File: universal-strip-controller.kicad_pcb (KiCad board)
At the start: 4 copper layers, 200 x 125 mm, 242 parts, among them J1 Conn_01x03_Pin, J10 DB301V-3.5-3P-GN, J11 DB301V-3.5-3P-GN, J12 DB301V-3.5-3P-GN, J13 DB301V-3.5-3P-GN, J14 DB301V-3.5-3P-GN, J15 DB301V-3.5-3P-GN, J16 DB301V-3.5-3P-GN, J17 DB301V-3.5-3P-GN, J18 DB301V-3.5-3P-GN, J19 DB301V-3.5-3P-GN, J2 Conn_01x02_Pin, J20 DB301V-3.5-3P-GN, J21 DB301V-3.5-3P-GN, J22 DB301V-3.5-3P-GN, J23 DB301V-3.5-3P-GN, J24 DB301V-3.5-3P-GN, J25 DB301V-3.5-3P-GN, J26 DB301V-3.5-3P-GN, J27 DB301V-3.5-3P-GN, J28 DB301V-3.5-3P-GN, J29 DB301V-3.5-3P-GN, J3 DBT50G-9.5-2P, J30 DB301V-3.5-3P-GN, J31 DB301V-3.5-3P-GN, J32 DB301V-3.5-3P-GN, J33 DB301V-3.5-3P-GN, J34 DB301V-3.5-3P-GN, J35 DB301V-3.5-3P-GN, J36 DB301V-3.5-3P-GN, J37 DB301V-3.5-3P-GN, J38 2.54-1*4, J39 DB301V-3.5-3P-GN, J4 DBT50G-9.5-2P, J5 DBT50G-9.5-2P, J6 DBT50G-9.5-2P, J7 DB301V-3.5-3P-GN, J8 DB301V-3.5-3P-GN, J9 DB301V-3.5-3P-GN, SW1 434133025816, SW2 434133025816, U1 RP2350B, U10 SN74LVC8T245PWR, U11 SN74LVC8T245PWR, U2 RPI RM2, U3 W25Q128JVSIQ, U4 SN74LVC1T45DBV, U5 TPS63070RNMR, U7 SN74LVC8T245PWR, U8 SN74LVC8T245PWR, U9 DS3231SN, X1 12MHz

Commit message: Some changes, not sure what...
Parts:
- moved D5 233.7 mm to (215.6, 57.2)
- moved D6 233.7 mm to (215.6, 61.8)
- moved D7 233.7 mm to (215.6, 66.3)
- moved D8 233.7 mm to (215.6, 70.9)
- moved BT1 17.3 mm to (194.2, 121.1)
- moved C118 17.3 mm to (172.8, 116.5)
- moved R95 17.3 mm to (191.6, 113.3)
- moved R96 17.3 mm to (172.8, 113.0)
- moved U9 17.3 mm to (180.5, 120.0)
- moved R94 17.3 mm to (188.3, 113.3)
- moved R49 10.8 mm to (154.9, 121.3)
- moved R50 10.8 mm to (156.5, 121.3)
- moved R53 10.8 mm to (161.4, 121.3)
- moved R54 10.8 mm to (163.0, 121.3)
- moved R47 10.8 mm to (151.6, 121.3)
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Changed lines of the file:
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@@
 		(capping no)
 		(filling no)
-		(zone_defaults)
 		(pcbplotparams
 			(layerselection 0x00000000_00000000_55555555_5755f5ff)
@@
 	(footprint "PCM_JLCPCB:D_SMA"
 		(layer "F.Cu")
-		(at -18.045 57.825)
+		(at 215.6 61.8)
 		(descr "Diode SMA (DO-214AC)")
 		(tags "Diode SMA (DO-214AC)")
@@
 	(footprint "PixelBlit:R_0603"
 		(layer "F.Cu")
-		(at 208.1 108.06 90)
+		(at 191.6 113.34 90)
 		(descr "Resistor SMD 0603 (1608 Metric), square (rectangular) end terminal, IPC_7351 nominal, (Body size source: IPC-SM-782 page 72, https://www.pcb-3d.com/wordpress/wp-content/uploads/ipc-sm-782a_amendment_1_and_2.pdf), generated with kicad-footprint-generator")
 		(tags "resistor")
@@
 	(footprint "PixelBlit:R_0603"
 		(layer "F.Cu")
-		(at 189.3 107.71 90)
+		(at 172.8 112.99 90)
 		(descr "Resistor SMD 0603 (1608 Metric), square (rectangular) end terminal, IPC_7351 nominal, (Body size source: IPC-SM-782 page 72, https://www.pcb-3d.com/wordpress/wp-content/uploads/ipc-sm-782a_amendment_1_and_2.pdf), generated with kicad-footprint-generator")
 		(tags "resistor")
@@
 	(footprint "PixelBlit:R_0402"
 		(layer "F.Cu")
-		(at 100.428571 121.45 -90)
+		(at 105.578571 120.75 -90)
 		(descr "Resistor SMD 0402 (1005 Metric), square (rectangular) end terminal, IPC_7351 nominal, (Body size source: IPC-SM-782 page 72, https://www.pcb-3d.com/wordpress/wp-content/uploads/ipc-sm-782a_amendment_1_and_2.pdf), generated with kicad-footprint-generator")
 		(tags "resistor")
@@
 	(footprint "PixelBlit:R_0402"
 		(layer "F.Cu")
-		(at 163.938583 122.98 -90)
+		(at 153.238583 121.33 -90)
 		(descr "Resistor SMD 0402 (1005 Metric), square (rectangular) end terminal, IPC_7351 nominal, (Body size source: IPC-SM-782 page 72, https://www.pcb-3d.com/wordpress/wp-content/uploads/ipc-sm-782a_amendment_1_and_2.pdf), generated with kicad-footprint-generator")
 		(tags "resistor")
@@
 	(footprint "PixelBlit:R_0402"
 		(layer "F.Cu")
-		(at 105.95 121.45 -90)
+		(at 111.1 120.75 -90)
 		(descr "Resistor SMD 0402 (1005 Metric), square (rectangular) end terminal, IPC_7351 nominal, (Body size source: IPC-SM-782 page 72, https://www.pcb-3d.com/wordpress/wp-content/uploads/ipc-sm-782a_amendment_1_and_2.pdf), generated with kicad-footprint-generator")
 		(tags "resistor")
@@
 	(footprint "PCM_JLCPCB:D_SMA"
 		(layer "F.Cu")
-		(at -18.045 62.375)
+		(at 215.6 66.35)
 		(descr "Diode SMA (DO-214AC)")
 		(tags "Diode SMA (DO-214AC)")
@@
 	(footprint "PixelBlit:R_0402"
 		(layer "F.Cu")
-		(at 165.567155 122.98 -90)
+		(at 154.867155 121.33 -90)
 		(descr "Resistor SMD 0402 (1005 Metric), square (rectangular) end terminal, IPC_7351 nominal, (Body size source: IPC-SM-782 page 72, https://www.pcb-3d.com/wordpress/wp-content/uploads/ipc-sm-782a_amendment_1_and_2.pdf), generated with kicad-footprint-generator")
 		(tags "resistor")
@@
 	(footprint "PixelBlit:R_0402"
 		(layer "F.Cu")
-		(at 104.55 121.45 -90)
+		(at 109.7 120.75 -90)
 		(descr "Resistor SMD 0402 (1005 Metric), square (rectangular) end terminal, IPC_7351 nominal, (Body size source: IPC-SM-782 page 72, https://www.pcb-3d.com/wordpress/wp-content/uploads/ipc-sm-782a_amendment_1_and_2.pdf), generated with kicad-footprint-generator")
 		(tags "resistor")
@@
 	(footprint "PixelBlit:R_0402"
 		(layer "F.Cu")
-		(at 108.8 121.45 -90)
+		(at 113.95 120.75 -90)
 		(descr "Resistor SMD 0402 (1005 Metric), square (rectangular) end terminal, IPC_7351 nominal, (Body size source: IPC-SM-782 page 72, https://www.pcb-3d.com/wordpress/wp-content/uploads/ipc-sm-782a_amendment_1_and_2.pdf), generated with kicad-footprint-generator")
 		(tags "resistor")
@@
 	(footprint "PixelBlit:R_0402"
 		(layer "F.Cu")
-		(at 168.824298 122.98 -90)
+		(at 158.124298 121.33 -90)
 		(descr "Resistor SMD 0402 (1005 Metric), square (rectangular) end terminal, IPC_7351 nominal, (Body size source: IPC-SM-782 page 72, https://www.pcb-3d.com/wordpress/wp-content/uploads/ipc-sm-782a_amendment_1_and_2.pdf), generated with kicad-footprint-generator")
 		(tags "resistor")
@@
 	(footprint "PixelBlit:R_0402"
 		(layer "F.Cu")
-		(at 101.907143 121.45 -90)
+		(at 107.057143 120.75 -90)
 		(descr "Resistor SMD 0402 (1005 Metric), square (rectangular) end terminal, IPC_7351 nominal, (Body size source: IPC-SM-782 page 72, https://www.pcb-3d.com/wordpress/wp-content/uploads/ipc-sm-782a_amendment_1_and_2.pdf), generated with kicad-footprint-generator")
 		(tags "resistor")
@@
 	(footprint "Package_SO:SOIC-16W_7.5x10.3mm_P1.27mm"
 		(layer "F.Cu")
-		(at 197 114.745)
+		(at 180.5 120.025)
 		(descr "SOIC, 16 Pin (JEDEC MS-013AA, https://www.analog.com/media/en/package-pcb-resources/package/pkg_pdf/soic_wide-rw/rw_16.pdf)")
 		(tags "SOIC SO")
@@
 	(footprint "PixelBlit:R_0402"
 		(layer "F.Cu")
-		(at 167.195726 122.98 -90)
+		(at 156.495726 121.33 -90)
 		(descr "Resistor SMD 0402 (1005 Metric), square (rectangular) end terminal, IPC_7351 nominal, (Body size source: IPC-SM-782 page 72, https://www.pcb-3d.com/wordpress/wp-content/uploads/ipc-sm-782a_amendment_1_and_2.pdf), generated with kicad-footprint-generator")
 		(tags "resistor")
@@
 	(footprint "PixelBlit:R_0402"
 		(layer "F.Cu")
-		(at 98.95 121.45 -90)
+		(at 104.1 120.75 -90)
 		(descr "Resistor SMD 0402 (1005 Metric), square (rectangular) end terminal, IPC_7351 nominal, (Body size source: IPC-SM-782 page 72, https://www.pcb-3d.com/wordpress/wp-content/uploads/ipc-sm-782a_amendment_1_and_2.pdf), generated with kicad-footprint-generator")
 		(tags "resistor")
@@
 	(footprint "PixelBlit:VQFN-HR-15_L3.0-W2.5-P0.50-BL_TPS63070RNMR"
 		(layer "F.Cu")
-		(at -19.02 116.655)
+		(at -14.45 119.88)
 		(property "Reference" "U5"
 			(at -2.75 -1.57 90)
@@
 	(footprint "PCM_JLCPCB:D_SMA"
 		(layer "F.Cu")
-		(at -18.045 53.275)
+		(at 215.6 57.25)
 		(descr "Diode SMA (DO-214AC)")
 		(tags "Diode SMA (DO-214AC)")
@@
 	(footprint "PixelBlit:R_0402"
 		(layer "F.Cu")
-		(at 172.081441 122.98 -90)
+		(at 161.381441 121.33 -90)
 		(descr "Resistor SMD 0402 (1005 Metric), square (rectangular) end terminal, IPC_7351 nominal, (Body size source: IPC-SM-782 page 72, https://www.pcb-3d.com/wordpress/wp-content/uploads/ipc-sm-782a_amendment_1_and_2.pdf), generated with kicad-footprint-generator")
 		(tags "resistor")
@@
 	(footprint "PixelBlit:R_0402"
 		(layer "F.Cu")
-		(at 107.3 121.45 -90)
+		(at 112.45 120.75 -90)
 		(descr "Resistor SMD 0402 (1005 Metric), square (rectangular) end terminal, IPC_7351 nominal, (Body size source: IPC-SM-782 page 72, https://www.pcb-3d.com/wordpress/wp-content/uploads/ipc-sm-782a_amendment_1_and_2.pdf), generated with kicad-footprint-generator")
 		(tags "resistor")
@@
 	(footprint "PixelBlit:C_0402"
 		(layer "F.Cu")
-		(at 189.3 111.2 90)
+		(at 172.8 116.48 90)
 		(descr "Capacitor SMD 0402 (1005 Metric), square (rectangular) end terminal, IPC_7351 nominal, (Body size source: IPC-SM-782 page 76, https://www.pcb-3d.com/wordpress/wp-content/uploads/ipc-sm-782a_amendment_1_and_2.pdf), generated with kicad-footprint-generator")
 		(tags "capacitor")
@@
 	(footprint "PixelBlit:TSSOP-24_L7.8-W4.4-P0.65-LS6.4-BL"
 		(layer "F.Cu")
-		(at 167.440012 114.2 180)
+		(at 156.740012 112.55 180)
 		(property "Reference" "U11"
 			(at -4.95 -2.64 90)
@@
 	(footprint "KiCad_Standard:Battery_Panasonic_CR1220-VCN_Vertical_CircularHoles"
 		(layer "F.Cu")
-		(at 210.75 115.85)
+		(at 194.25 121.13)
 		(descr "Panasonic CR-1220/VCN battery, https://industrial.panasonic.com/cdbs/www-data/pdf2/AAA4000/AAA4000D140.PDF")
 		(tags "battery CR-1220 coin cell vertical")
@@
 	(footprint "PixelBlit:TSSOP-24_L7.8-W4.4-P0.65-LS6.4-BL"
 		(layer "F.Cu")
-		(at 104.38 112.77 180)
+		(at 109.53 112.07 180)
 		(property "Reference" "U10"
 			(at -4.95 -2.64 90)
@@
 	(footprint "PixelBlit:R_0402"
 		(layer "F.Cu")
-		(at 170.452869 122.98 -90)
+		(at 159.752869 121.33 -90)
 		(descr "Resistor SMD 0402 (1005 Metric), square (rectangular) end terminal, IPC_7351 nominal, (Body size source: IPC-SM-782 page 72, https://www.pcb-3d.com/wordpress/wp-content/uploads/ipc-sm-782a_amendment_1_and_2.pdf), generated with kicad-footprint-generator")
 		(tags "resistor")
@@
 	(footprint "PixelBlit:R_0402"
 		(layer "F.Cu")
-		(at 173.710012 122.98 -90)
+		(at 163.010012 121.33 -90)
 		(descr "Resistor SMD 0402 (1005 Metric), square (rectangular) end terminal, IPC_7351 nominal, (Body size source: IPC-SM-782 page 72, https://www.pcb-3d.com/wordpress/wp-content/uploads/ipc-sm-782a_amendment_1_and_2.pdf), generated with kicad-footprint-generator")
 		(tags "resistor")
@@
 	(footprint "PixelBlit:R_0402"
 		(layer "F.Cu")
-		(at 103.2 121.45 -90)
+		(at 108.35 120.75 -90)
 		(descr "Resistor SMD 0402 (1005 Metric), square (rectangular) end terminal, IPC_7351 nominal, (Body size source: IPC-SM-782 page 72, https://www.pcb-3d.com/wordpress/wp-content/uploads/ipc-sm-782a_amendment_1_and_2.pdf), generated with kicad-footprint-generator")
 		(tags "resistor")
@@
 	(footprint "PixelBlit:R_0402"
 		(layer "F.Cu")
-		(at 162.310012 122.98 -90)
+		(at 151.610012 121.33 -90)
 		(descr "Resistor SMD 0402 (1005 Metric), square (rectangular) end terminal, IPC_7351 nominal, (Body size source: IPC-SM-782 page 72, https://www.pcb-3d.com/wordpress/wp-content/uploads/ipc-sm-782a_amendment_1_and_2.pdf), generated with kicad-footprint-generator")
 		(tags "resistor")
@@
 	(footprint "PCM_JLCPCB:D_SMA"
 		(layer "F.Cu")
-		(at -18.045 66.925)
+		(at 215.6 70.9)
 		(descr "Diode SMA (DO-214AC)")
 		(tags "Diode SMA (DO-214AC)")
@@
 	(footprint "PixelBlit:R_0603"
 		(layer "F.Cu")
-		(at 204.8 108.04 90)
+		(at 188.3 113.32 90)
 		(descr "Resistor SMD 0603 (1608 Metric), square (rectangular) end terminal, IPC_7351 nominal, (Body size source: IPC-SM-782 page 72, https://www.pcb-3d.com/wordpress/wp-content/uploads/ipc-sm-782a_amendment_1_and_2.pdf), generated with kicad-footprint-generator")
 		(tags "resistor")

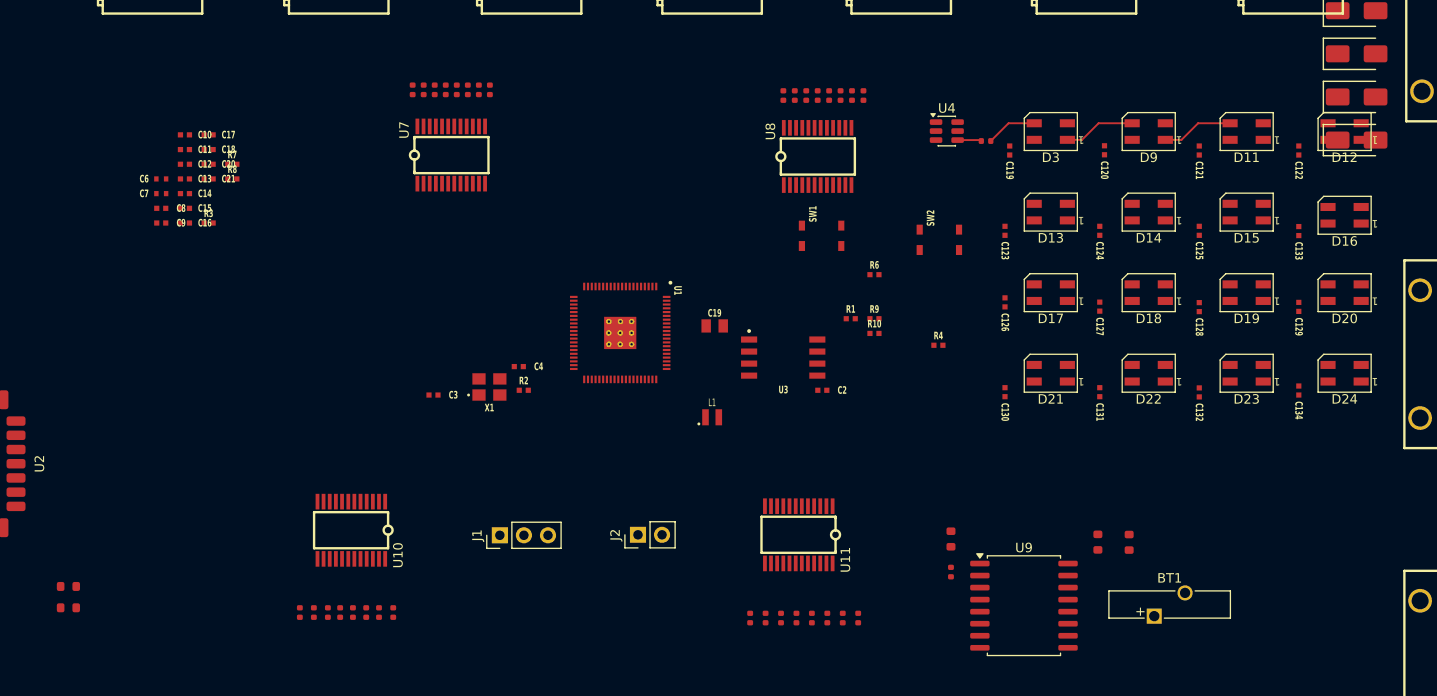
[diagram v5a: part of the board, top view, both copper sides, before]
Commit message: Did away with the status LEDs for now, too much real estate
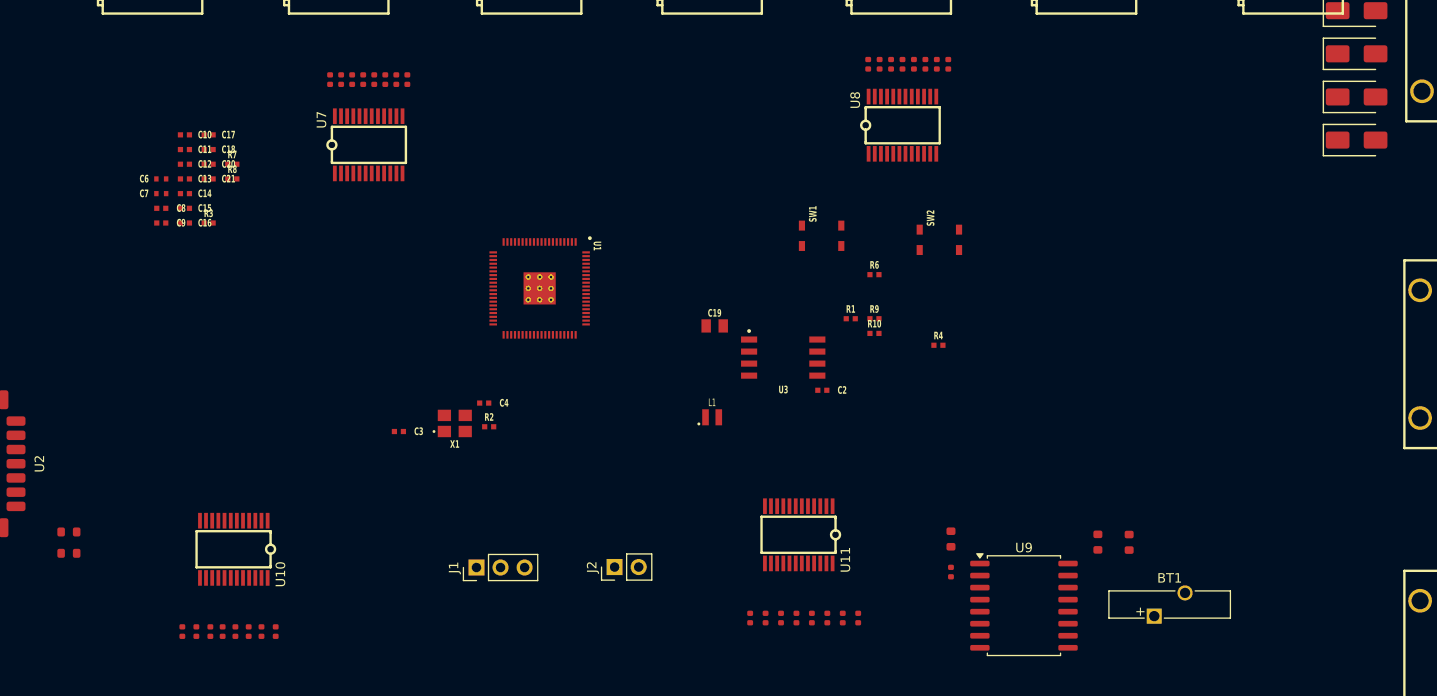
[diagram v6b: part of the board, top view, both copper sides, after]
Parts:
- removed C119, C120, C121, C122, C123, C124, C125, C126, C127, C128, C129, C130, C131, C132, C133, C134: 100n, RPI_COMPILED:generic_capc1005x50
- removed D11, D12, D13, D14, D15, D16, D17, D18, D19, D20, D21, D22, D23, D24, D3, D9: SK6812MINI, LED_SMD:LED_SK6812MINI_PLCC4_3.5x3.5mm_P1.75mm
- removed R19: 47Ω, PixelBlit:R_0402
- removed U4: SN74LVC1T45DBV, Package_TO_SOT_SMD:SOT-23-6
- moved R43 12.6 mm to (97.3, 122.8)
- moved R45 12.6 mm to (100.0, 122.8)
- moved R46 12.6 mm to (101.5, 122.8)
- moved U10 12.6 mm to (97.1, 114.1)
- moved R39 12.6 mm to (91.7, 122.8)
- moved R40 12.6 mm to (93.2, 122.8)
- moved R41 12.6 mm to (94.7, 122.8)
- moved R42 12.6 mm to (96.0, 122.8)
- moved R44 12.6 mm to (98.7, 122.8)
- moved U1 9.71 mm to (129.4, 86.5)
- moved R28 9.54 mm to (166.5, 62.9)
- moved R29 9.54 mm to (165.3, 62.9)
- moved R30 9.54 mm to (164.1, 62.9)
- moved U8 9.54 mm to (167.7, 69.3)
- moved R21 9.54 mm to (172.5, 62.9)
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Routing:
- net Net-(D11-DIN): track 7.56 -> 0.00 mm
- net Net-(D3-DOUT): track 7.56 -> 0.00 mm
- net Net-(D3-DIN): track 5.36 -> 0.00 mm
- net Net-(U4-B): track 2.54 -> 0.00 mm

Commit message: Working out the layout
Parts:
- moved L2 242.2 mm to (205.9, 95.0)
- moved D10 226.9 mm to (205.8, 81.5)
- moved D4 223.2 mm to (196.1, 80.1)
- moved C23 222.1 mm to (201.1, 62.1)
- moved C24 222.1 mm to (201.1, 65.1)
- moved C25 222.1 mm to (200.8, 48.2)
- moved C28 222.1 mm to (187.7, 94.9)
- moved C31 222.1 mm to (200.8, 59.4)
- moved C32 222.1 mm to (201.1, 68.2)
- moved C33 222.1 mm to (201.1, 71.2)
- moved PWR_LED2 222.1 mm to (179.9, 92.4)
- moved R14 222.1 mm to (194.2, 89.0)
- moved R17 222.1 mm to (191.0, 90.3)
- moved TP3 220.1 mm to (188.8, 97.5)
- moved R13 218.5 mm to (186.9, 82.2)
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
